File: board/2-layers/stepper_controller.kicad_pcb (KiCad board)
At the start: 4 copper layers, 99 x 46 mm, 109 parts, among them J201 USB_OTG, P103 M3_AOUT, P104 M3_BOUT, P105 M2_AOUT, P106 M2_BOUT, P107 M1_AOUT, P108 M1_BOUT, P201 UART1, P301 12V_Conn, U101 DRV8825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

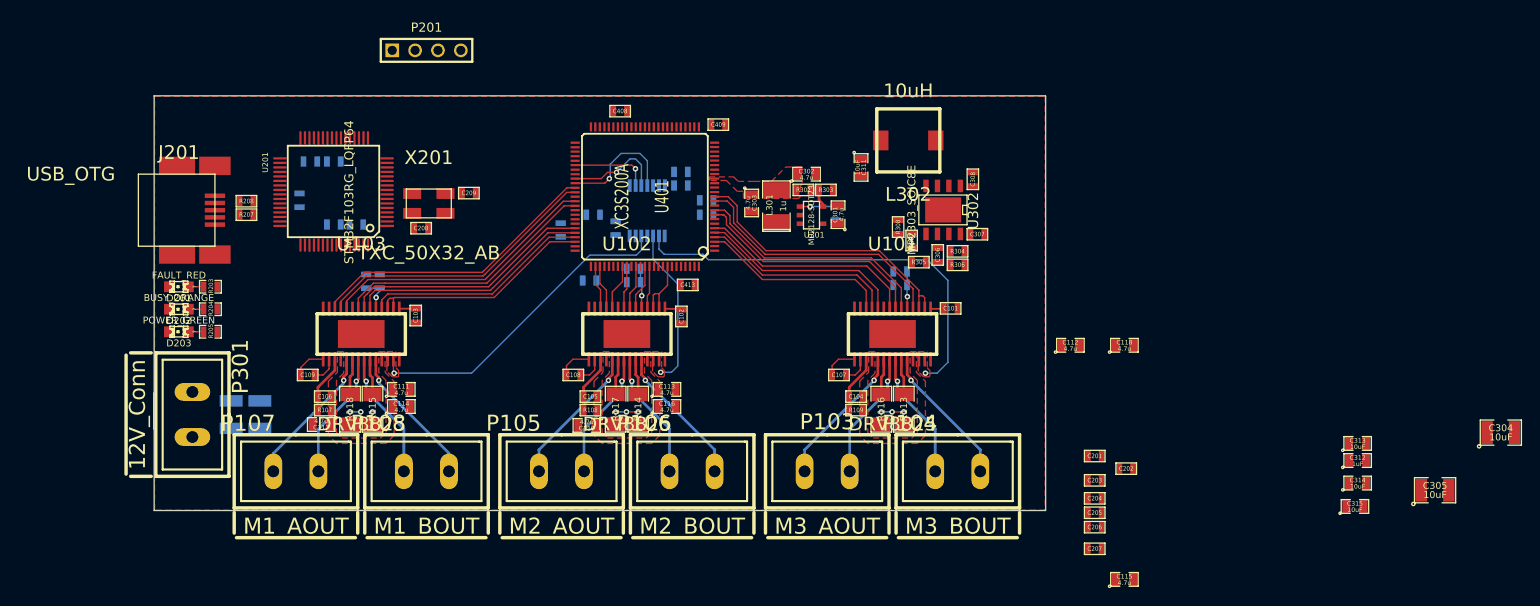
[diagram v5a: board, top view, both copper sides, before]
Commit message: added decoupling capacitor + 4 pin connector
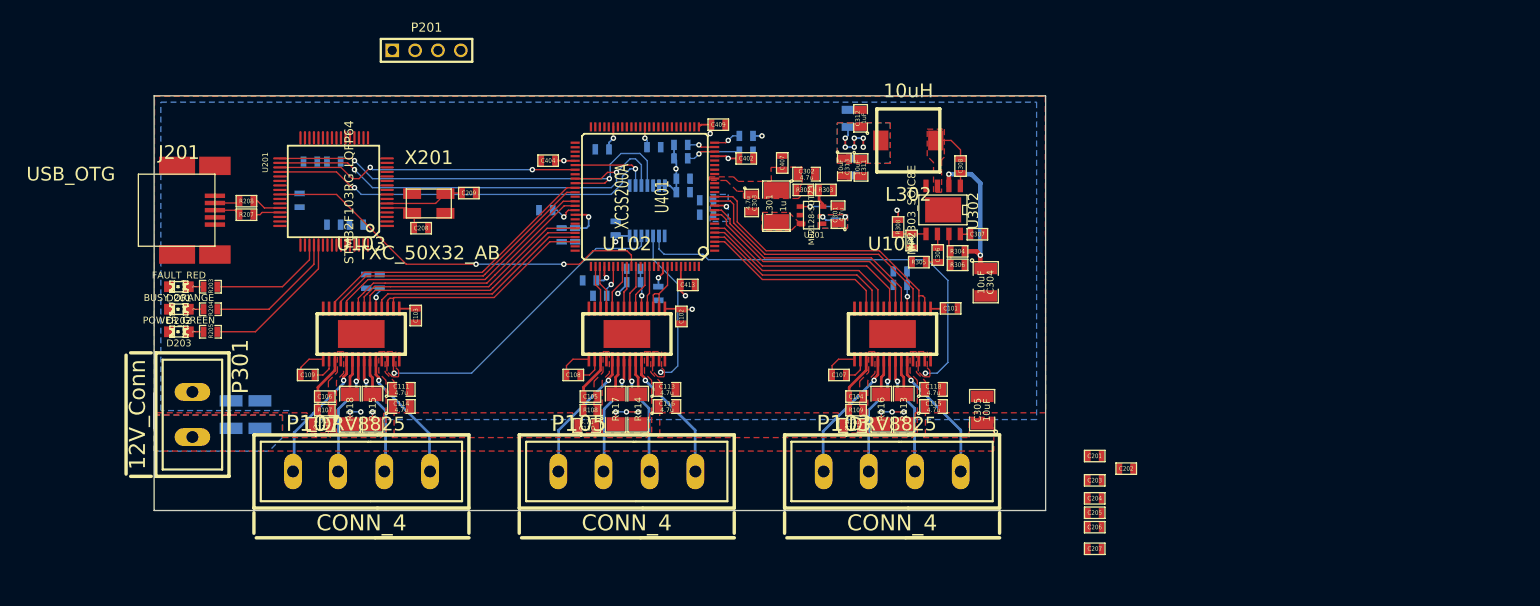
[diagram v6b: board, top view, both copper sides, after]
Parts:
- removed P104: M3_BOUT, MOL_CONN_2_VH
- removed P106: M2_BOUT, MOL_CONN_2_VH
- removed P108: M1_BOUT, MOL_CONN_2_VH
- added C401: 1u, SM0603, B.Cu at (160.8, 92.0)
- added C402: 1u, SM0603, F.Cu at (171.0, 93.2)
- added C403: 100n, SM0603, B.Cu at (154.8, 108.5)
- added C404: 100n, SM0603, F.Cu at (149.0, 93.5)
- added C405: 100n, SM0603, B.Cu at (148.8, 99.0)
- added C406: 10n, SM0603, B.Cu at (161.2, 108.2)
- added C407: 10n, SM0603, F.Cu at (175.0, 93.8)
- added R401: R, SM0603, B.Cu at (171.0, 90.8)
- added R402: R, SM0603, B.Cu at (163.8, 93.2)
- added R403: NE, SM0603, B.Cu at (171.0, 92.5)
- added R404: R, SM0603, B.Cu at (163.8, 91.8)
- C314, C315, C408: moved to B.Cu
- P103: value M3_AOUT -> CONN_4; footprint MOL_CONN_2_VH -> MOL_CONN_4_VH
- P105: value M2_AOUT -> CONN_4; footprint MOL_CONN_2_VH -> MOL_CONN_4_VH
- P107: value M1_AOUT -> CONN_4; footprint MOL_CONN_2_VH -> MOL_CONN_4_VH
- moved C314 69.6 mm to (182.3, 88.8), turned to 90 degrees
- moved C315 67.3 mm to (182.8, 94.2), turned to 270 degrees
- moved C312 67.0 mm to (183.7, 88.8), turned to 90 degrees
- moved C313 64.7 mm to (181.9, 94.2), turned to 270 degrees
- moved C304 59.6 mm to (197.6, 107.0), turned to 270 degrees
- moved C305 51.1 mm to (197.2, 121.2), turned to 90 degrees
- moved C115 28.6 mm to (191.8, 120.8)
- moved C112 25.8 mm to (182.8, 122.9), turned to 180 degrees
- moved C118 21.8 mm to (191.8, 118.9)
- moved P107 7.27 mm to (128.3, 128.0)
- moved P105 7.23 mm to (157.7, 128.0)
- moved P103 7.20 mm to (187.2, 128.0)
- moved C408 4.70 mm to (155.0, 92.2), turned to 180 degrees
- moved C410 3.01 mm to (152.0, 101.8), turned to 270 degrees
- moved C308 2.01 mm to (194.8, 94.1)
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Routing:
- net +3.3V: track 5.18 -> 55.2 mm, vias 0 -> 23
- net /STM32/FPGA_CLK: track 0.00 -> 44.3 mm, vias 0 -> 2
- net /FPGA/COM_MOSI: track 8.74 -> 50.9 mm, vias 1 -> 2
- net /FPGA/COM_CLK: track 10.8 -> 50.7 mm, vias 1 -> 2
- net /FPGA/COM_CS: track 13.3 -> 50.9 mm, vias 1 -> 2
- net /FPGA/COM_MISO: track 0.00 -> 33.9 mm, vias 0 -> 2
- net +12V: track 0.00 -> 16.9 mm, vias 0 -> 2
- net N-0000095: track 0.00 -> 16.8 mm
- net N-0000097: track 0.00 -> 14.9 mm
- net N-0000099: track 0.00 -> 13.1 mm
- net +1.2V: track 0.00 -> 9.16 mm, vias 0 -> 3
- net N-00000116: track 0.00 -> 8.79 mm
- net N-00000156: track 0.00 -> 7.89 mm, vias 0 -> 1
- net N-00000117: track 0.00 -> 4.78 mm
- net /PSU/DC_SW: track 0.00 -> 4.22 mm
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- added copper zone on B.Cu, net +12V
- added copper zone on POWER, net +12V
- added copper zone on B.Cu, net +3.3V
- added copper zone on F.Cu, net +3.3V
- added copper zone on POWER, net +3.3V
- added copper zone on F.Cu, net /PSU/1.2_SW
- added copper zone on F.Cu, net /PSU/DC_SW
- added copper zone on B.Cu, net GND

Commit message: routing crap
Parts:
- C207: moved to B.Cu
- moved C203 97.6 mm to (120.1, 90.2), turned to 90 degrees
- moved C202 97.6 mm to (118.9, 102.6), turned to 270 degrees
- moved C204 91.2 mm to (129.2, 88.3)
- moved C205 83.9 mm to (134.9, 94.7)
- moved C201 82.7 mm to (129.9, 104.6)
- moved C207 70.6 mm to (153.4, 94.0)
- moved C206 62.4 mm to (167.9, 87.9)
- moved R206 0.76 mm to (122.0, 98.3)
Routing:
- net /STM32/FPGA_INITB: track 0.00 -> 33.5 mm, vias 0 -> 2
- net /STM32//CLR_DAC: track 0.00 -> 32.8 mm, vias 0 -> 1
- net /FPGA/DIN: track 0.00 -> 28.2 mm, vias 0 -> 2
- net /FPGA/CCLK: track 0.00 -> 26.2 mm
- net /FPGA/DONE: track 0.00 -> 24.2 mm, vias 0 -> 2
- net +3.3V: track 55.2 -> 69.1 mm, vias 23 -> 24
- net /STM32/BOOT1: track 0.00 -> 3.77 mm, vias 0 -> 1
- net /STM32/USB_PUP: track 0.00 -> 3.35 mm, vias 0 -> 1
- net /STM32/BOOT0: track 0.00 -> 3.27 mm, vias 0 -> 1
- net D+: track 3.06 -> 6.02 mm, vias 0 -> 1

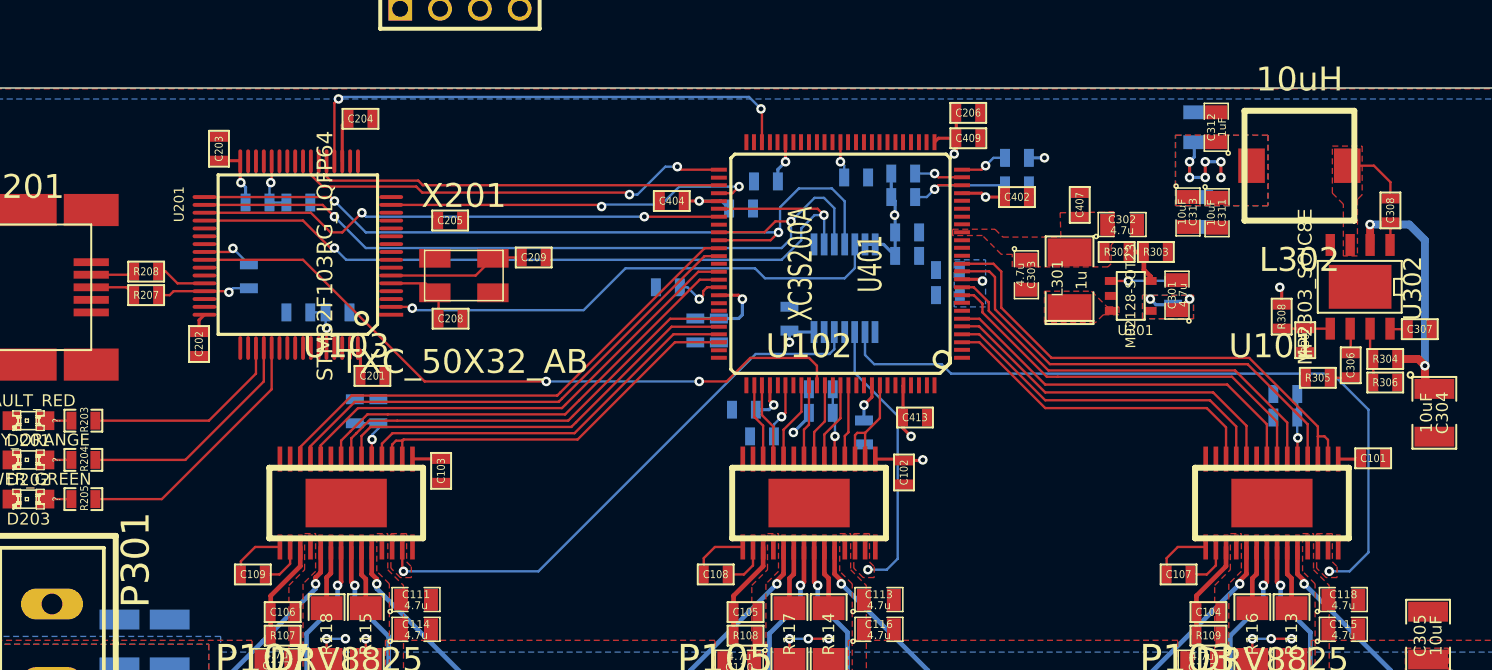
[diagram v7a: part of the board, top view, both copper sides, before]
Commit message: added fixing hole - capacitor on vref
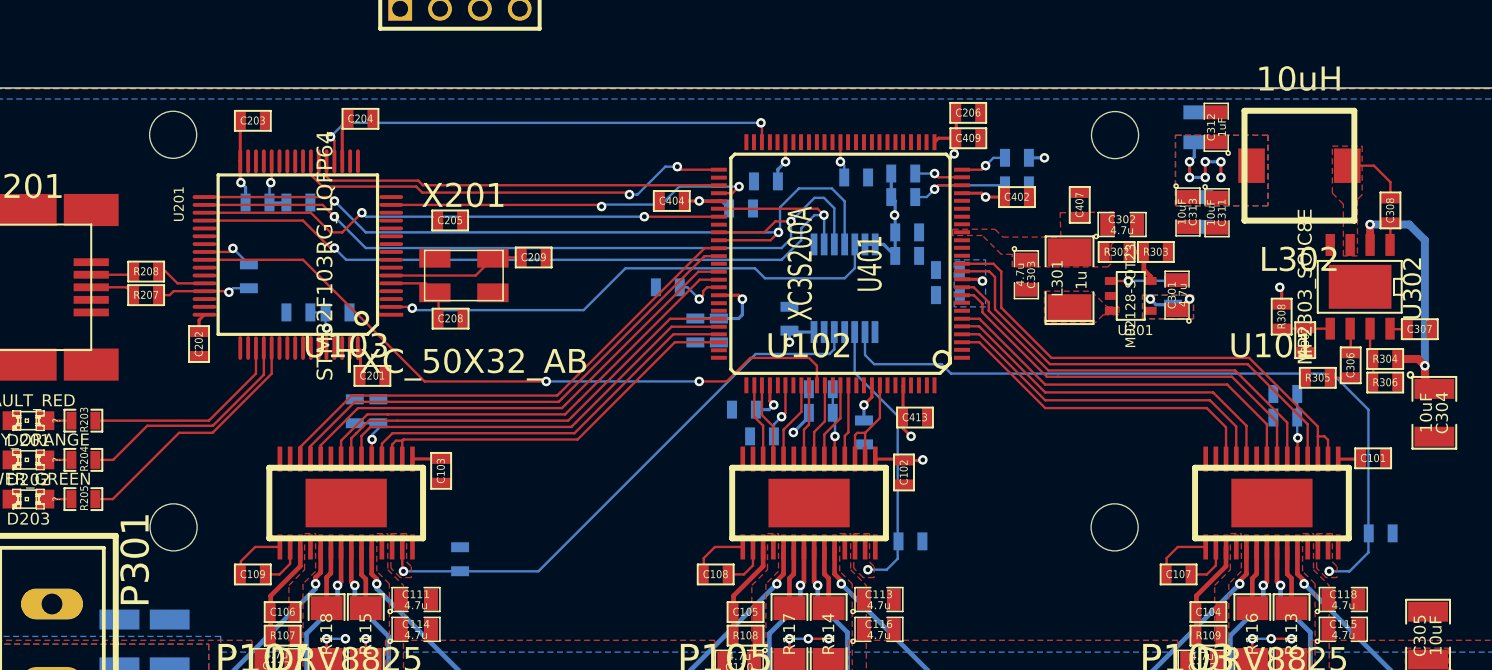
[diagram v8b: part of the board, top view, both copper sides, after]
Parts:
- added 3mm_nonplated: VAL**, 3mm_nonplated, F.Cu at (117.2, 89.3)
- added 3mm_nonplated: VAL**, 3mm_nonplated, F.Cu at (177.2, 89.3)
- added 3mm_nonplated: VAL**, 3mm_nonplated, F.Cu at (177.2, 114.3)
- added 3mm_nonplated: VAL**, 3mm_nonplated, F.Cu at (117.2, 114.3)
- added C122: 100n, SM0603, B.Cu at (135.5, 116.3)
- added C123: 100n, SM0603, B.Cu at (164.2, 115.2)
- added C124: 100n, SM0603, B.Cu at (194.2, 114.7)
- moved C203 2.80 mm to (122.3, 88.4), turned to 0 degrees
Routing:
- net /STM32/FPGA_INITB: track 33.5 -> 30.7 mm
- net +3.3V: track 69.1 -> 70.3 mm
- net N-0000095: track 16.8 -> 16.2 mm
